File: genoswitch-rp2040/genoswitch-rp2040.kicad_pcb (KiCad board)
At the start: 2 copper layers, 37 parts, among them J1 USB_B_Micro, J2 Conn_01x03_Socket-PicoDebug, J3 HW-SPI0, J4 HW-SPI1, J5 PIO-SPI0, J6 PIO-SPI1, J7 SERIAL, SW1 PTS815_SJM_250_SMTR_LFS, U1 NCP1117-3.3_SOT223, U2 W25Q128JVS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

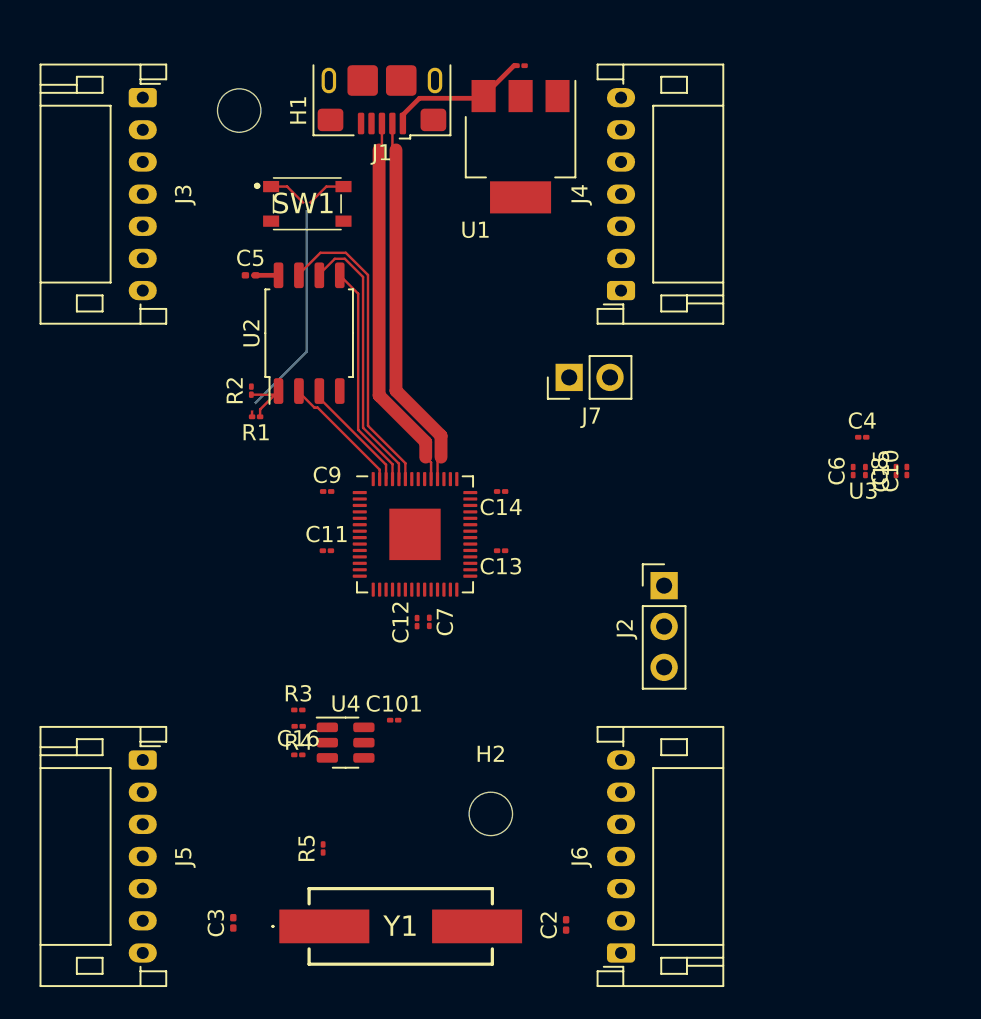
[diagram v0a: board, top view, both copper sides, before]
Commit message: Add ADC Channel sockets x4, place on board 5mil apart
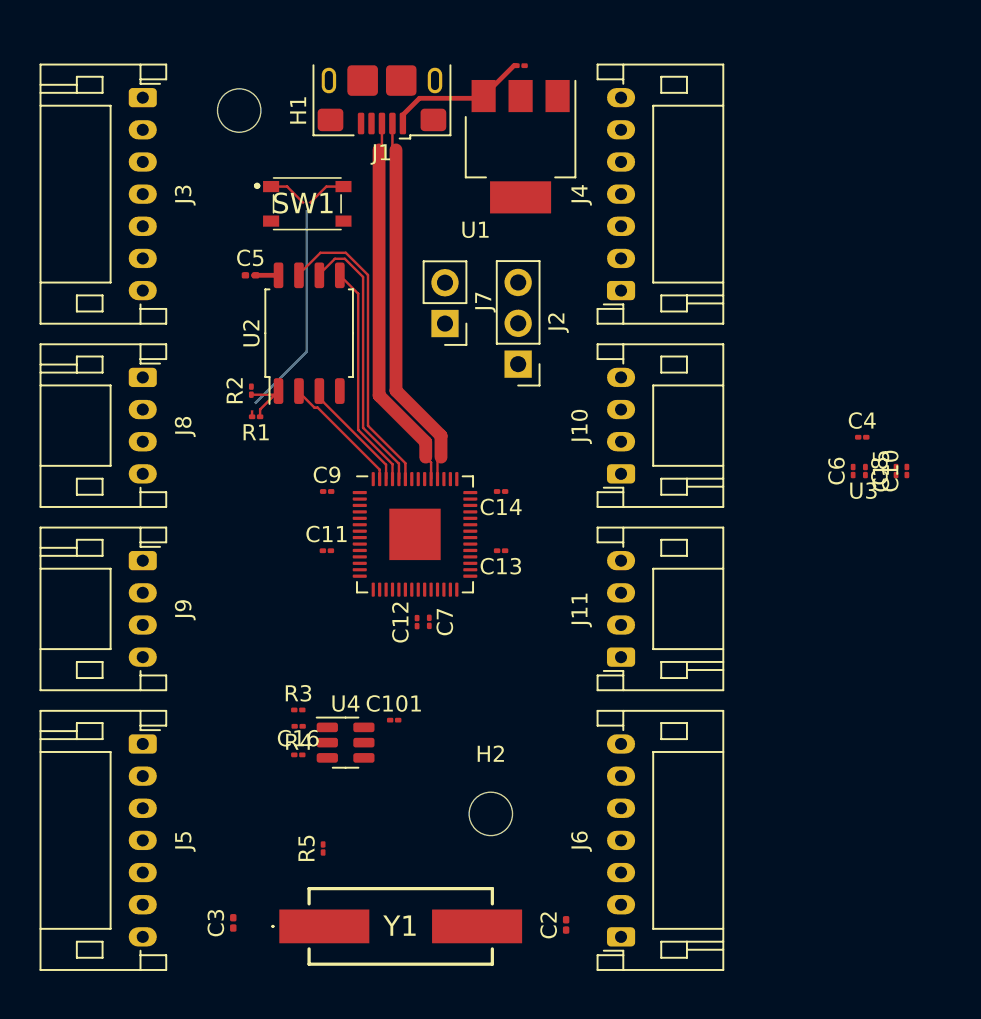
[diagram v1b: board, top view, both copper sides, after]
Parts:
- added J10: RP2040_ADC2, Connector_JST:JST_PH_S4B-PH-K_1x04_P2.00mm_Horizontal, F.Cu at (122.2, 70.2)
- added J11: RP2040_ADC3, Connector_JST:JST_PH_S4B-PH-K_1x04_P2.00mm_Horizontal, F.Cu at (122.2, 81.5)
- added J8: RP2040_ADC0, Connector_JST:JST_PH_S4B-PH-K_1x04_P2.00mm_Horizontal, F.Cu at (92.4, 64.2)
- added J9: RP2040_ADC1, Connector_JST:JST_PH_S4B-PH-K_1x04_P2.00mm_Horizontal, F.Cu at (92.4, 75.5)
- moved J2 16.5 mm to (115.8, 63.3), turned to 180 degrees
- moved J7 8.42 mm to (111.2, 60.8), turned to 180 degrees
- moved J5 1.00 mm to (92.4, 87.0)
- moved J6 1.00 mm to (122.2, 99.0)
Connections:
- U3 pad 38: unconnected-(U3-GPIO26_ADC0-Pad38) -> /GPIO26_ADC0
- U3 pad 39: unconnected-(U3-GPIO27_ADC1-Pad39) -> /GPIO27_ADC1
- U3 pad 40: unconnected-(U3-GPIO28_ADC2-Pad40) -> /GPIO28_ADC2
- U3 pad 41: unconnected-(U3-GPIO29_ADC3-Pad41) -> /GPIO29_ADC3
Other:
- board text added: ".5mm"

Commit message: Update PCB from schematic for new 0602 sizing
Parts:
- C1, C10, C101, C11, C12, C13, C14, C15, C16, C4, C6, C7, C8, C9: footprint Capacitor_SMD:C_01005_0402Metric -> Capacitor_SMD:C_0201_0603Metric
- R1, R2, R3, R4, R5: footprint Resistor_SMD:R_01005_0402Metric -> Resistor_SMD:R_0201_0603Metric

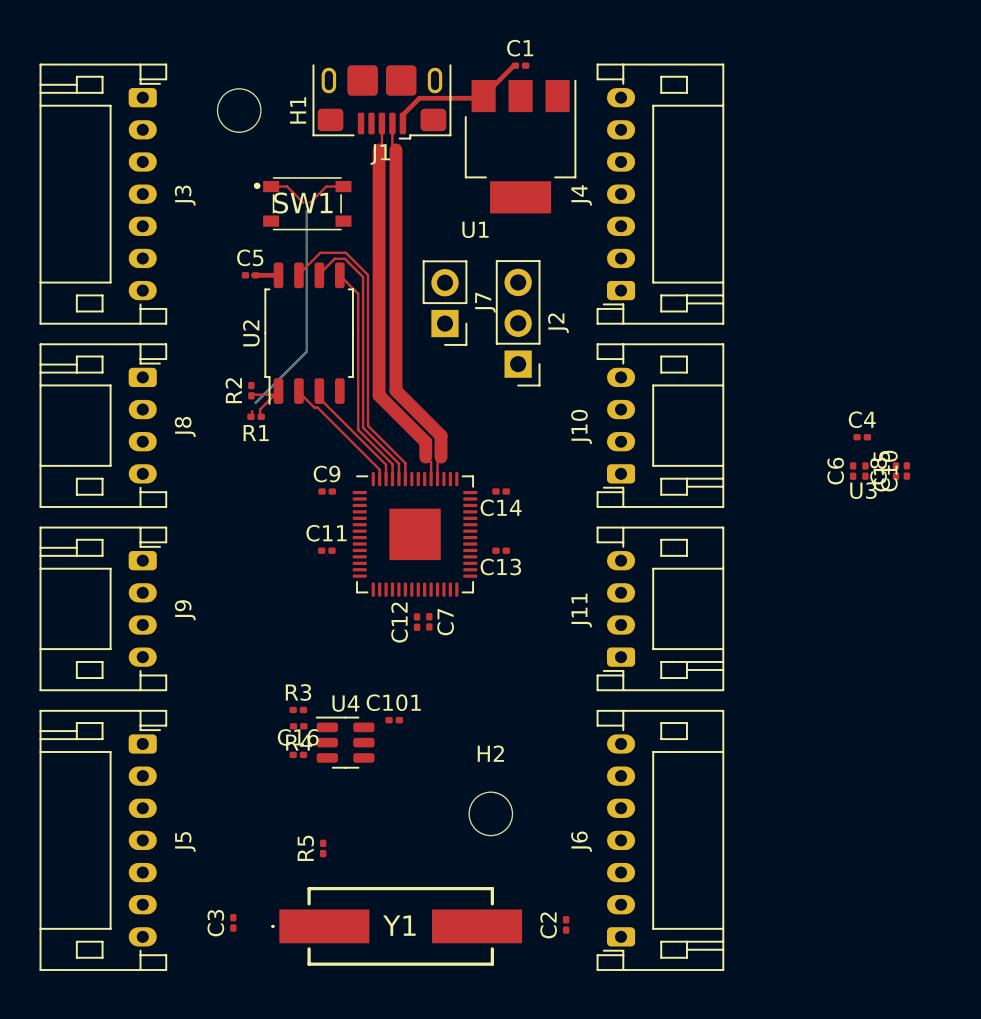
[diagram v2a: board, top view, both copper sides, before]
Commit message: Set board outline
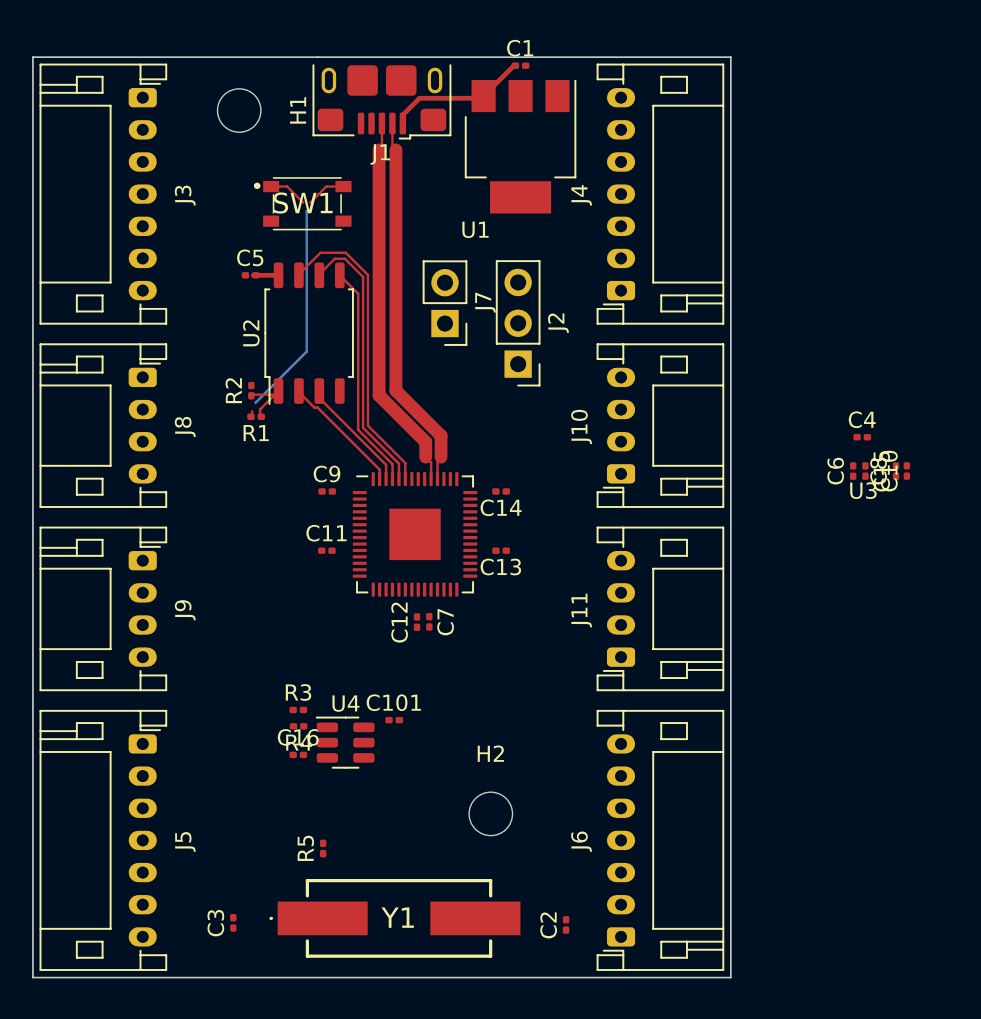
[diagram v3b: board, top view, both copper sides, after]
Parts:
- moved Y1 0.51 mm to (108.4, 97.8)
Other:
- board outline added: 43.4 x 57.3 mm
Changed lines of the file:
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@@
   )
   (footprint "ABLS-12.000MHZ-B4-T:ABLS" (layer "F.Cu")
-    (at 108.458 98.298)
+    (at 108.352 97.8)
     (descr "ABLS")
     (tags "Crystal or Oscillator")
@@
     )
   )
+  (gr_line (start 128.992 44.23) (end 128.992 101.48)
+    (stroke (width 0.1) (type default)) (layer "Edge.Cuts"))
+  (gr_line (start 103.282 44.23) (end 85.582 44.23)
+    (stroke (width 0.1) (type default)) (layer "Edge.Cuts"))
+  (gr_line (start 103.282 44.23) (end 128.992 44.23)
+    (stroke (width 0.1) (type default)) (layer "Edge.Cuts"))
+  (gr_line (start 85.582 101.48) (end 85.582 44.23)
+    (stroke (width 0.1) (type default)) (layer "Edge.Cuts"))
+  (gr_line (start 128.992 101.48) (end 85.582 101.48)
+    (stroke (width 0.1) (type default)) (layer "Edge.Cuts"))
   (gr_line (start 87.112 50.165) (end 87.112 99.695)
     (stroke (width 0.15) (type default)) (layer "User.1"))

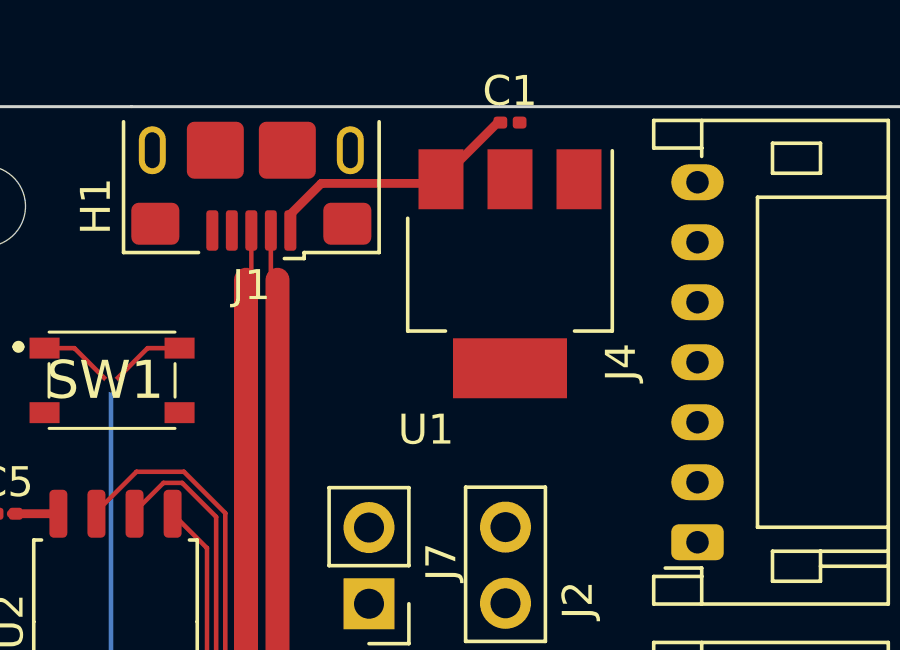
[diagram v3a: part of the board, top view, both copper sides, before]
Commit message: Move U1 down slightly
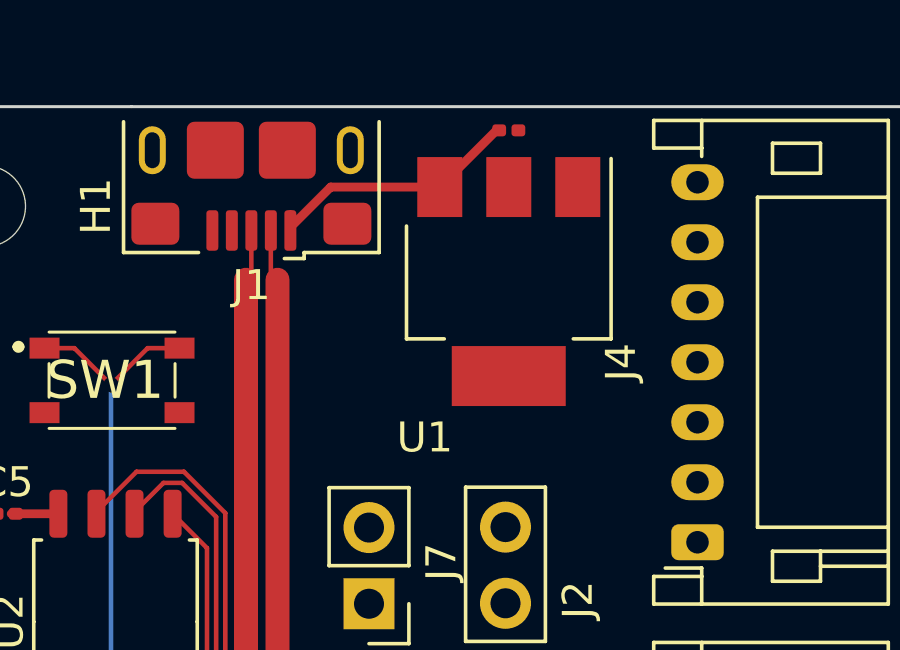
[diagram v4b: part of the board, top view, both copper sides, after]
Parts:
- moved C1 0.26 mm to (115.9, 45.0)
- moved U1 0.26 mm to (115.9, 50.1)
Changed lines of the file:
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@@
   )
   (footprint "Package_TO_SOT_SMD:SOT-223-3_TabPin2" (layer "F.Cu")
-    (at 115.912 49.8 -90)
+    (at 115.872 50.06 -90)
     (descr "module CMS SOT223 4 pins")
     (tags "CMS SOT")
@@
   )
   (footprint "Capacitor_SMD:C_0201_0603Metric" (layer "F.Cu")
-    (at 115.912 44.76)
+    (at 115.872 45.02)
     (descr "Capacitor SMD 0201 (0603 Metric), square (rectangular) end terminal, IPC_7351 nominal, (Body size source: https://www.vishay.com/docs/20052/crcw0201e3.pdf), generated with kicad-footprint-generator")
     (tags "capacitor")
@@
     (property "ki_keywords" "cap capacitor")
     (attr smd)
-    (fp_text reference "C1" (at 0 -1.05) (layer "F.SilkS")
+    (fp_text reference "C1" (at 0 -1.05) (layer "F.SilkS") hide
         (effects (font (size 1 1) (thickness 0.15)))
     )
@@
     (effects (font (size 1 1) (thickness 0.15)) (justify left bottom))
   )
-  (segment (start 115.502 44.76) (end 113.612 46.65) (width 0.295656) (layer "F.Cu") (net 1))
+  (segment (start 115.462 45.02) (end 113.572 46.91) (width 0.295656) (layer "F.Cu") (net 1))
   (segment (start 108.59 47.822) (end 108.59 48.358) (width 0.295656) (layer "F.Cu") (net 1))
-  (segment (start 113.612 46.65) (end 113.47286 46.78914) (width 0.295656) (layer "F.Cu") (net 1))
-  (segment (start 113.47286 46.78914) (end 109.62286 46.78914) (width 0.295656) (layer "F.Cu") (net 1))
-  (segment (start 115.662 44.76) (end 115.502 44.76) (width 0.295656) (layer "F.Cu") (net 1))
-  (segment (start 109.62286 46.78914) (end 108.59 47.822) (width 0.295656) (layer "F.Cu") (net 1))
+  (segment (start 109.93486 46.91) (end 108.59 48.25486) (width 0.295656) (layer "F.Cu") (net 1))
+  (segment (start 113.572 46.91) (end 113.43286 47.04914) (width 0.295656) (layer "F.Cu") (net 1))
+  (segment (start 113.572 46.91) (end 109.93486 46.91) (width 0.295656) (layer "F.Cu") (net 1))
+  (segment (start 115.622 45.02) (end 115.462 45.02) (width 0.295656) (layer "F.Cu") (net 1))
+  (segment (start 108.59 48.25486) (end 108.59 48.358) (width 0.295656) (layer "F.Cu") (net 1))
   (segment (start 100.857 57.8) (end 99.287 57.8) (width 0.295656) (layer "F.Cu") (net 5))
   (segment (start 111.544 70.4735) (end 111.547 70.4765) (width 0.15) (layer "F.Cu") (net 7))

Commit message: Update PCB from schematic (see prev commit)
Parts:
- added C16: 100nF, Capacitor_SMD:C_0201_0603Metric, F.Cu at (133.2, 74.2)
- renumbered C16 to C17, C101 to C18
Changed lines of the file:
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@@
+    )
+  )
+  (footprint "Capacitor_SMD:C_0201_0603Metric" (layer "F.Cu")
+    (at 133.197 74.24)
+    (descr "Capacitor SMD 0201 (0603 Metric), square (rectangular) end terminal, IPC_7351 nominal, (Body size source: https://www.vishay.com/docs/20052/crcw0201e3.pdf), generated with kicad-footprint-generator")
+    (tags "capacitor")
+    (property "Sheetfile" "genoswitch-rp2040.kicad_sch")
+    (property "Sheetname" "")
+    (property "ki_description" "Unpolarized capacitor")
+    (property "ki_keywords" "cap capacitor")
+    (attr smd)
+    (fp_text reference "C16" (at 0 -1.05) (layer "F.SilkS")
+        (effects (font (size 1 1) (thickness 0.15)))
+    )
+    (fp_text value "100nF" (at 0 1.05) (layer "F.Fab")
+        (effects (font (size 1 1) (thickness 0.15)))
+    )
+    (fp_text user "${REFERENCE}" (at 0 -0.68) (layer "F.Fab")
+        (effects (font (size 0.25 0.25) (thickness 0.04)))
+    )
+    (fp_line (start -0.7 -0.35) (end 0.7 -0.35)
+      (stroke (width 0.05) (type solid)) (layer "F.CrtYd"))
+    (fp_line (start -0.7 0.35) (end -0.7 -0.35)
+      (stroke (width 0.05) (type solid)) (layer "F.CrtYd"))
+    (fp_line (start 0.7 -0.35) (end 0.7 0.35)
+      (stroke (width 0.05) (type solid)) (layer "F.CrtYd"))
+    (fp_line (start 0.7 0.35) (end -0.7 0.35)
+      (stroke (width 0.05) (type solid)) (layer "F.CrtYd"))
+    (fp_line (start -0.3 -0.15) (end 0.3 -0.15)
+      (stroke (width 0.1) (type solid)) (layer "F.Fab"))
+    (fp_line (start -0.3 0.15) (end -0.3 -0.15)
+      (stroke (width 0.1) (type solid)) (layer "F.Fab"))
+    (fp_line (start 0.3 -0.15) (end 0.3 0.15)
+      (stroke (width 0.1) (type solid)) (layer "F.Fab"))
+    (fp_line (start 0.3 0.15) (end -0.3 0.15)
+      (stroke (width 0.1) (type solid)) (layer "F.Fab"))
+    (pad "" smd roundrect (at -0.345 0) (size 0.318 0.36) (layers "F.Paste") (roundrect_rratio 0.25))
+    (pad "" smd roundrect (at 0.345 0) (size 0.318 0.36) (layers "F.Paste") (roundrect_rratio 0.25))
+    (pad "1" smd roundrect (at -0.32 0) (size 0.46 0.4) (layers "F.Cu" "F.Mask") (roundrect_rratio 0.25)
+      (net 5 "+3V3") (pintype "passive"))
+    (pad "2" smd roundrect (at 0.32 0) (size 0.46 0.4) (layers "F.Cu" "F.Mask") (roundrect_rratio 0.25)
+      (net 2 "GND") (pintype "passive"))
+    (model "${KICAD6_3DMODEL_DIR}/Capacitor_SMD.3dshapes/C_0201_0603Metric.wrl"
+      (offset (xyz 0 0 0))
+      (scale (xyz 1 1 1))
+      (rotate (xyz 0 0 0))
     )
   )
@@
     (property "ki_keywords" "cap capacitor")
     (attr smd)
-    (fp_text reference "C101" (at 0 -1.05) (layer "F.SilkS")
+    (fp_text reference "C18" (at 0 -1.05) (layer "F.SilkS")
         (effects (font (size 1 1) (thickness 0.15)))
     )
@@
     (property "ki_keywords" "cap capacitor")
     (attr smd)
-    (fp_text reference "C16" (at 0 -1.05) (layer "F.SilkS")
-        (effects (font (size 1 1) (thickness 0.15)))
-    )
+    (fp_text reference "C17" (at 0 -1.05) (layer "F.SilkS")
+        (effects (font (size 1 1) (thickness 0.15)))
+    )
